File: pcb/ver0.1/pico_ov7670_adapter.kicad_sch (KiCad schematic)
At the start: 17 parts, among them J1 GPIO Header, SW1 SW_Push, SW2 SW_Push, U1 CAMERA-OV7670, U2 RASPBERRY_PI_PICO_W

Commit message: updated layout changes as per the  feedback.
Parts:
- U2: footprint pico_ov7670_adapter:MODULE_RASPBERRY_PI_PICO_W -> pico_ov7670_adapter:RASPBERRY_PI_PICO_W
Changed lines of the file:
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@@
 			)
 		)
-		(property "Footprint" "pico_ov7670_adapter:MODULE_RASPBERRY_PI_PICO_W"
+		(property "Footprint" "pico_ov7670_adapter:RASPBERRY_PI_PICO_W"
 			(at 119.38 76.2 0)
 			(effects

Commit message: layout updated.
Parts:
- removed H4: MountingHole, MountingHole:MountingHole_3.2mm_M3_DIN965, symbol Mechanical:MountingHole
- added R6: 22R, Resistor_SMD:R_0603_1608Metric, symbol Device:R_Small
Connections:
- net OV_PCLK_PICO_IO9: now also R6.1; no longer U2.17 (UART0_RX/I2C0_SCL/SPI1_CSN/GP13)
- new net: R6.2, U2.17 (UART0_RX/I2C0_SCL/SPI1_CSN/GP13)
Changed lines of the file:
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@@
 	(wire
 		(pts
-			(xy 52.07 91.44) (xy 71.12 91.44)
+			(xy 52.07 91.44) (xy 58.42 91.44)
 		)
 		(stroke
@@
 	(wire
 		(pts
+			(xy 63.5 91.44) (xy 71.12 91.44)
+		)
+		(stroke
+			(width 0)
+			(type default)
+		)
+	)
+	(wire
+		(pts
 			(xy 52.07 96.52) (xy 71.12 96.52)
 		)
@@
 	)
 	(symbol
-		(lib_id "Mechanical:MountingHole")
-		(at 157.48 190.5 0)
+		(lib_id "power:+3V3")
+		(at 226.06 71.12 0)
 		(unit 1)
-		(exclude_from_sim yes)
-		(in_bom no)
+		(exclude_from_sim no)
+		(in_bom yes)
 		(on_board yes)
 		(dnp no)
-		(fields_autoplaced yes)
-		(property "Reference" "H4"
-			(at 160.02 189.2299 0)
+		(property "Reference" "#PWR010"
+			(at 226.06 74.93 0)
 			(effects
 				(font
 					(size 1.27 1.27)
 				)
-				(justify left)
+				(hide yes)
 			)
 		)
-		(property "Value" "MountingHole"
-			(at 160.02 191.7699 0)
+		(property "Value" "+3V3"
+			(at 226.06 67.564 0)
 			(effects
 				(font
 					(size 1.27 1.27)
 				)
-				(justify left)
 			)
 		)
-		(property "Footprint" "MountingHole:MountingHole_3.2mm_M3_DIN965"
-			(at 157.48 190.5 0)
+		(property "Footprint" ""
+			(at 226.06 71.12 0)
 			(effects
 				(font
@@
 			)
 		)
-		(property "Datasheet" "~"
-			(at 157.48 190.5 0)
+		(property "Datasheet" ""
+			(at 226.06 71.12 0)
 			(effects
 				(font
@@
 			)
 		)
-		(property "Description" "Mounting Hole without connection"
-			(at 157.48 190.5 0)
+		(property "Description" "Power symbol creates a global label with name \"+3V3\""
+			(at 226.06 71.12 0)
 			(effects
 				(font
@@
 			)
 		)
+		(pin "1"
+		)
 		(instances
 			(project "pico_ov7670_adapter"
 				(path "/8ca4dbff-a6fb-40ff-ba8a-6032e61c2093"
-					(reference "H4")
+					(reference "#PWR010")
 					(unit 1)
 				)
@@
 	)
 	(symbol
-		(lib_id "power:+3V3")
-		(at 226.06 71.12 0)
+		(lib_id "Device:R_Small")
+		(at 60.96 91.44 90)
 		(unit 1)
 		(exclude_from_sim no)
@@
 		(on_board yes)
 		(dnp no)
-		(property "Reference" "#PWR010"
-			(at 226.06 74.93 0)
+		(property "Reference" "R6"
+			(at 56.388 90.678 90)
 			(effects
 				(font
 					(size 1.27 1.27)
 				)
-				(hide yes)
 			)
 		)
-		(property "Value" "+3V3"
-			(at 226.06 67.564 0)
+		(property "Value" "22R"
+			(at 65.532 90.424 90)
 			(effects
 				(font
@@
 			)
 		)
-		(property "Footprint" ""
-			(at 226.06 71.12 0)
+		(property "Footprint" "Resistor_SMD:R_0603_1608Metric"
+			(at 60.96 91.44 0)
 			(effects
 				(font
@@
 			)
 		)
-		(property "Datasheet" ""
-			(at 226.06 71.12 0)
+		(property "Datasheet" "~"
+			(at 60.96 91.44 0)
 			(effects
 				(font
@@
 			)
 		)
-		(property "Description" "Power symbol creates a global label with name \"+3V3\""
-			(at 226.06 71.12 0)
+		(property "Description" "Resistor, small symbol"
+			(at 60.96 91.44 0)
 			(effects
 				(font
@@
 			)
 		)
+		(pin "2"
+		)
 		(pin "1"
 		)
@@
 			(project "pico_ov7670_adapter"
 				(path "/8ca4dbff-a6fb-40ff-ba8a-6032e61c2093"
-					(reference "#PWR010")
+					(reference "R6")
 					(unit 1)
 				)

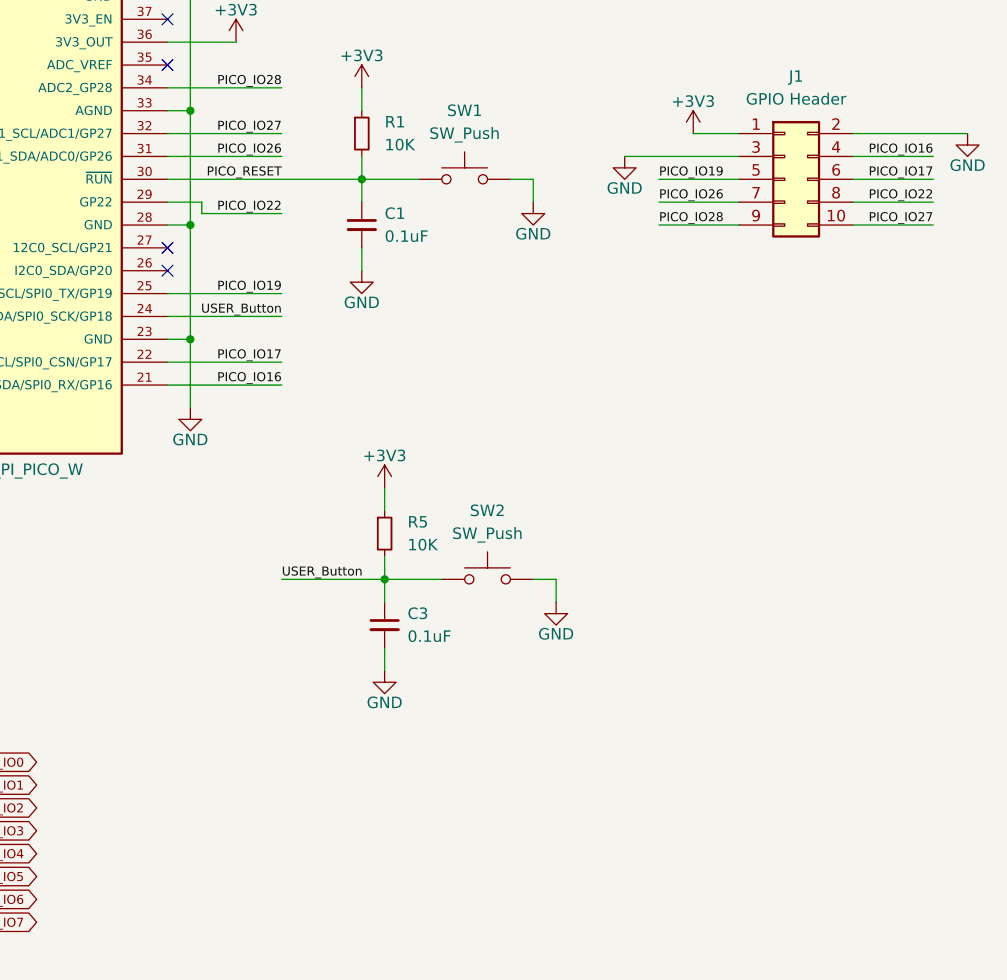
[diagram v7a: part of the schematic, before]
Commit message: layout updated as per the feedback.
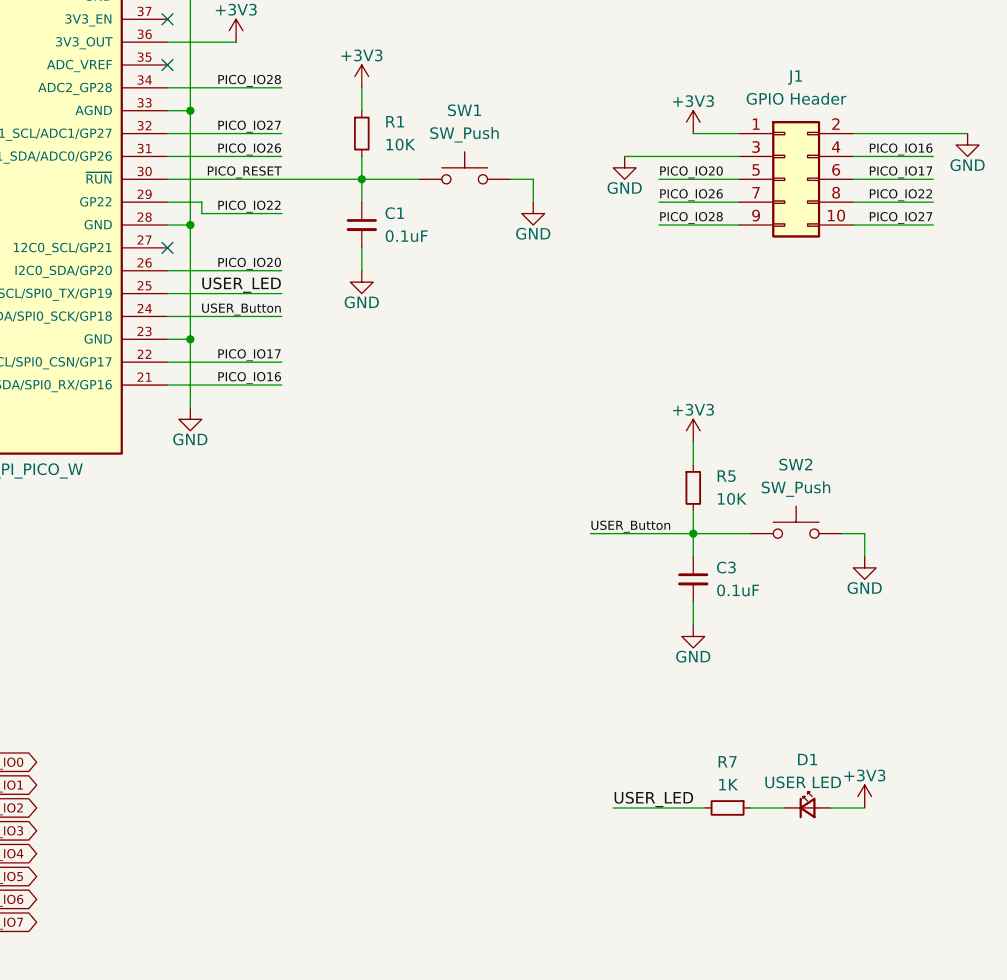
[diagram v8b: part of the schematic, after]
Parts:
- added D1: USER LED, LED_SMD:LED_0603_1608Metric, symbol Device:LED_Small
- added R7: 1K, Resistor_SMD:R_0603_1608Metric, symbol Device:R_Small
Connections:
- net +3V3: now also D1.2 (A)
- net PICO_IO20: now reaches U2.26 (I2C0_SDA/GP20)
- net PICO_IO20: now also J1.5 (Pin_5)
- net PICO_IO19 renamed USER_LED
- net USER_LED: now also R7.2; no longer J1.5 (Pin_5)
- new net: D1.1 (K), R7.1
- no-connect marks 15 -> 14
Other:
- moved on the sheet: C3, R5, SW2
